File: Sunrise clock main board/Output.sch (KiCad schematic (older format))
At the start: 20 parts, among them J2 Screw terminal/dnf, J3 Screw terminal/dnf, J4 Conn_02x05_Odd_Even, Q2 IRML2244, U7 74AHC125D

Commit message: Tweaks
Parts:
- F1: footprint Fuse:Fuse_1812_4532Metric_Pad1.30x3.40mm_HandSolder -> Fuse-fixed:Fuse_1812_4532Metric_Pad1.30x3.40mm_HandSolder
- L1: footprint Inductor-extra:L_12x12mm_H8mm-L_Radial_D10.0mm_P5.00mm -> Inductor-fixed:L_12x12mm_H8mm
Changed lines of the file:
@@
 F 0 "F1" V 7375 3100 50  0000 C CNN
 F 1 "Polyfuse 1.5A >=6V" V 7466 3100 50  0000 C CNN
-F 2 "Fuse:Fuse_1812_4532Metric_Pad1.30x3.40mm_HandSolder" H 7650 2900 50  0001 L CNN
+F 2 "Fuse-fixed:Fuse_1812_4532Metric_Pad1.30x3.40mm_HandSolder" H 7650 2900 50  0001 L CNN
 F 3 "~" H 7600 3100 50  0001 C CNN
 	1    7600 3100
@@
 F 0 "L1" V 6675 3100 50  0000 C CNN
 F 1 "22uH 3A" V 6584 3100 50  0000 C CNN
-F 2 "Inductor-extra:L_12x12mm_H8mm-L_Radial_D10.0mm_P5.00mm" H 6450 3100 50  0001 C CNN
+F 2 "Inductor-fixed:L_12x12mm_H8mm" H 6450 3100 50  0001 C CNN
 F 3 "~" H 6450 3100 50  0001 C CNN
 	1    6450 3100

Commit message: Now in stereo if you want.
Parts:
- removed J2: Screw terminal/dnf, TerminalBlock_Phoenix:TerminalBlock_Phoenix_MKDS-1,5-2-5.08_1x02_P5.08mm_Horizontal, symbol Connector:Screw_Terminal_01x02
- removed R63: 100k, Resistor_SMD:R_0805_2012Metric_Pad1.20x1.40mm_HandSolder, symbol Device:R
- added A4: max98357, Module-extra:max98357, symbol Module-extra:max98357
- added D5, D6: BAV99, Package_TO_SOT_SMD:SOT-23, symbol Diode:BAV99
- added Q1: IRML2244, Package_TO_SOT_SMD:SOT-23, symbol Device:Q_PMOS_GSD
- added Q3, Q4: 2N7002, Package_TO_SOT_SMD:SOT-23, symbol Transistor_FET:2N7002
- added R14, R16: 100R, Resistor_SMD:R_0805_2012Metric_Pad1.20x1.40mm_HandSolder, symbol Device:R
- added R62, R66, R69, R70: 100k, Resistor_SMD:R_0805_2012Metric_Pad1.20x1.40mm_HandSolder, symbol Device:R
- added R79: 560k, Resistor_SMD:R_0805_2012Metric_Pad1.20x1.40mm_HandSolder, symbol Device:R
- J3: footprint TerminalBlock_Phoenix:TerminalBlock_Phoenix_MKDS-1,5-3-5.08_1x03_P5.08mm_Horizontal -> TerminalBlock_Phoenix:TerminalBlock_Phoenix_MKDS-1,5-5-5.08_1x05_P5.08mm_Horizontal; symbol Connector:Screw_Terminal_01x03 -> Connector:Screw_Terminal_01x05
- NT1: footprint NetTie:NetTie-2_SMD_Pad0.5mm -> NetTie-fixed:NetTie-2_SMD_Pad0.5mm
- R63: renamed from R41; value 10k -> 100k
- renumbered R14 to R1
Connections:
- net labels added: EXTERNAL_GND, GPIO1, GPO2, GPO2_5V, I2S_GAIN0, I2S_GAIN1, ~SDL, ~SDR
- net labels removed: I2S_GAIN, NEOPIXEL_GND, SPK+, SPK-
- wire segments 92 -> 146
- no-connect marks 0 -> 5
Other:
- note added: "Audio amplifier module"
- note added: "Connect to pins 1 to 5\nof GX16-5 connector."
- note added: "Do not fit any components in this block if you want mono output"
- note added: "External interface for Neopixel and GP(I)O"
- note added: "Unused, but not forgotten"
- note added: "left channel or mono"
- note added: "right channel\n"
- note removed: "Connect to pin 1,2 and 3\nof GX16-5 connector."
- note removed: "MAX98357 I2S 3W audio amplifier module"
- note removed: "Neopixel"
- moved on the sheet: A3, C3, D3, D4, F1, J4, L1, NT1, Q2, R3, R4, R63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

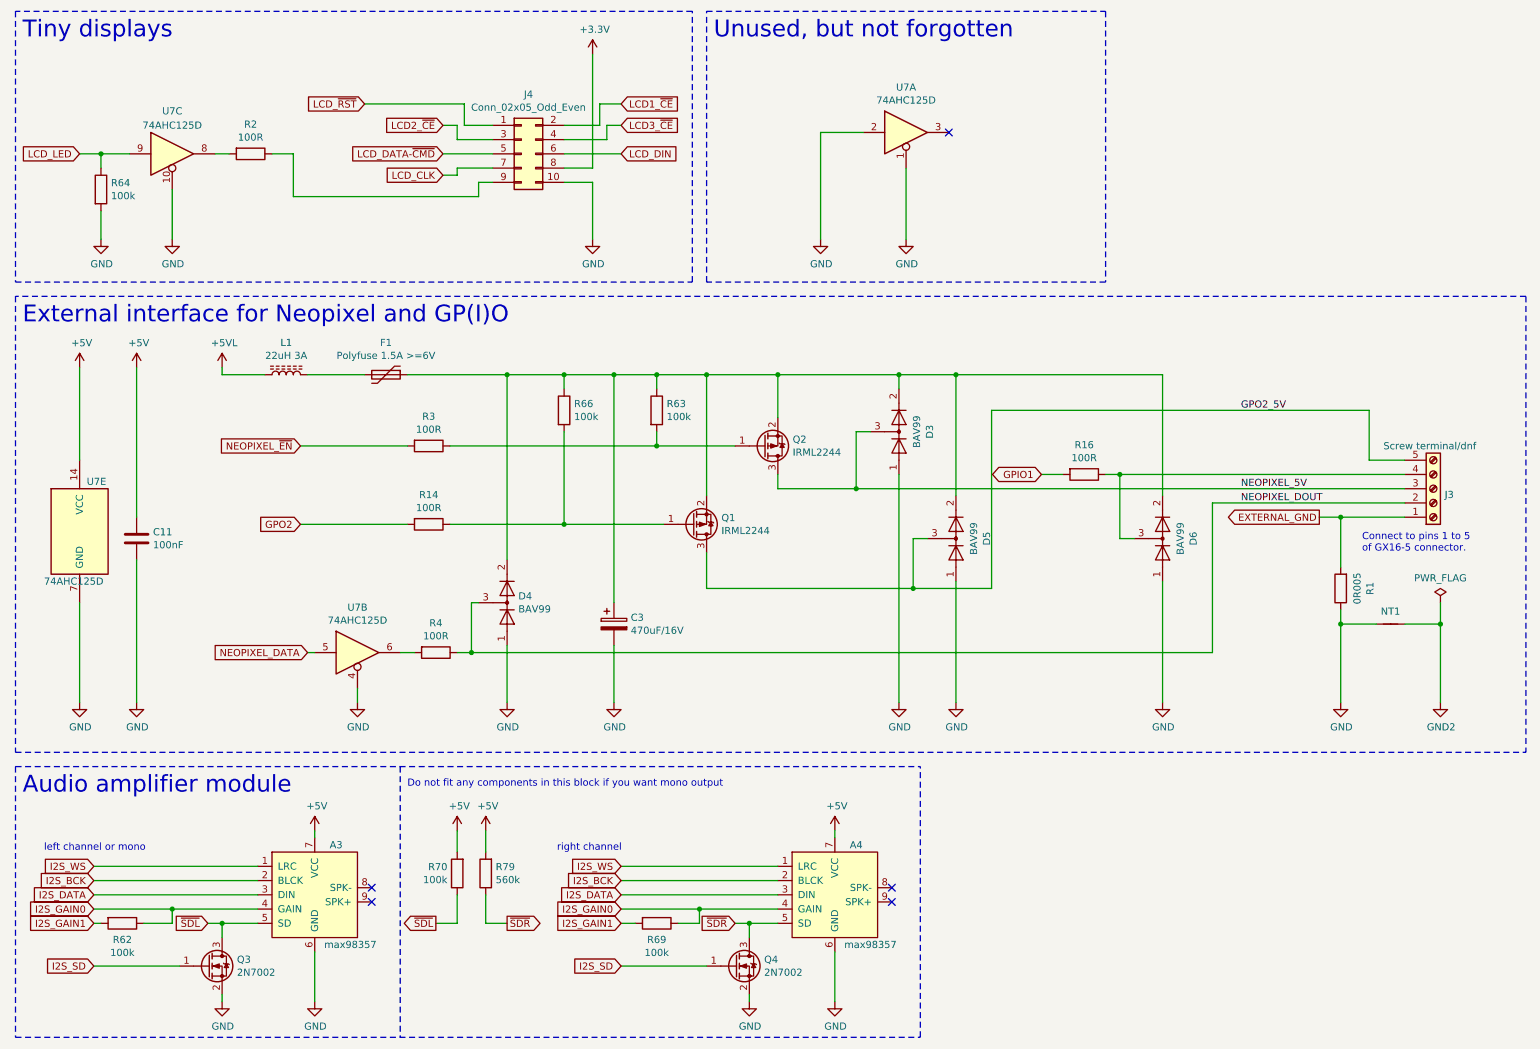
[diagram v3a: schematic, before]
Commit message: Started with checklist.
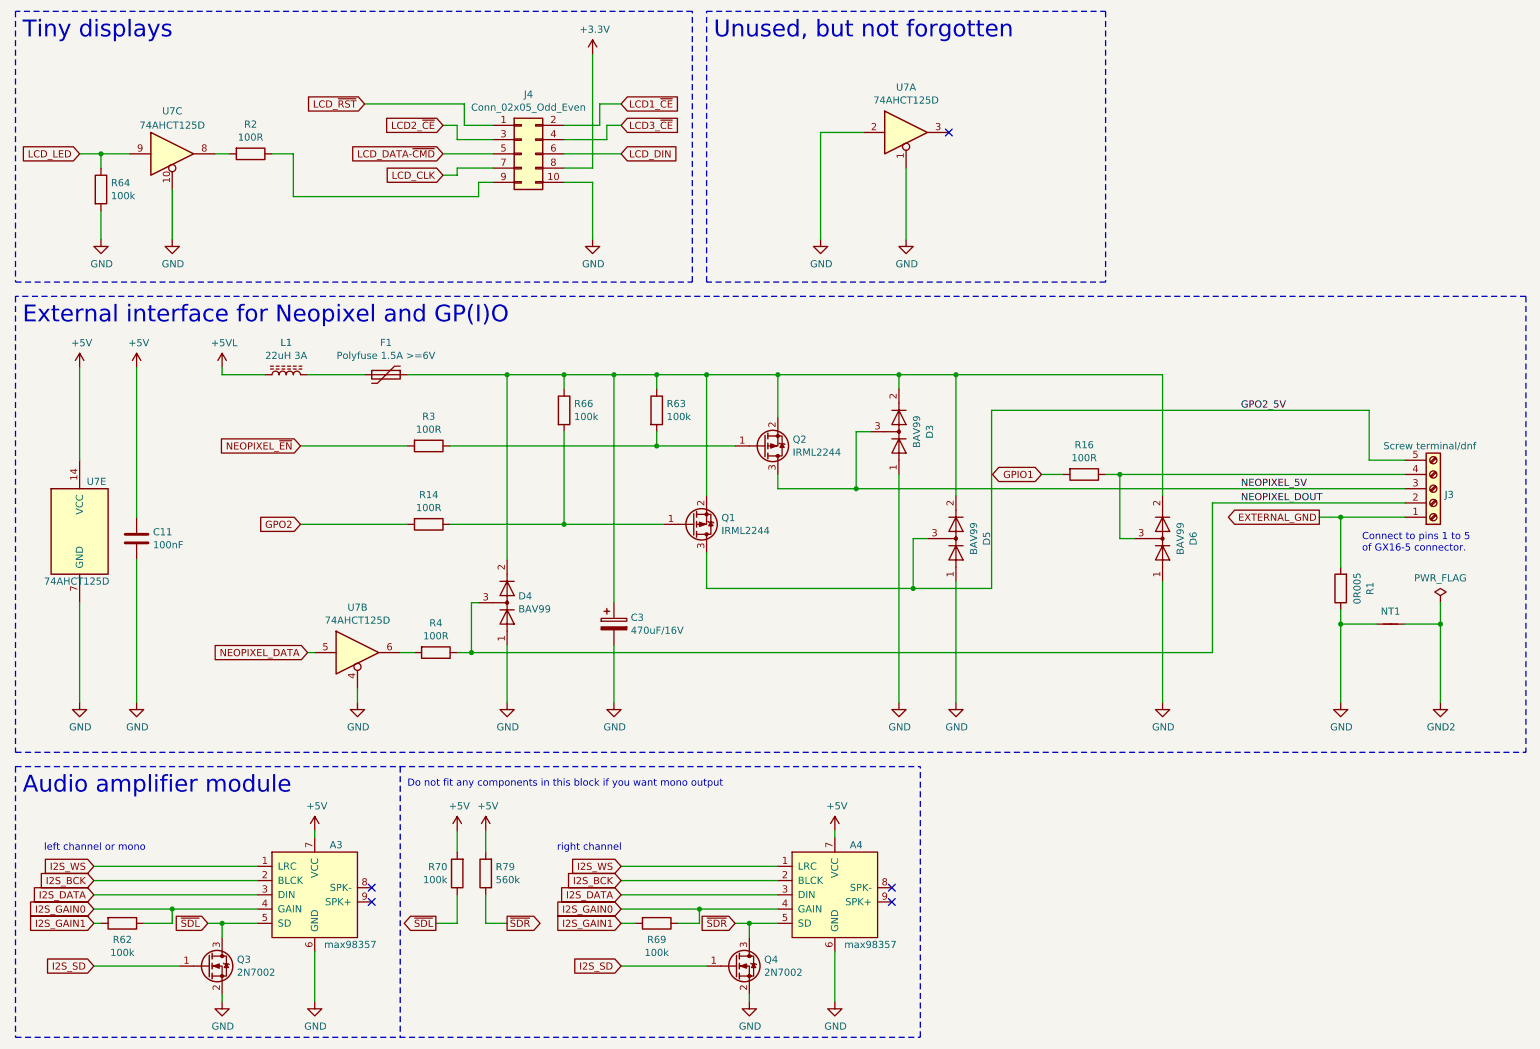
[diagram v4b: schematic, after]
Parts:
- U7: value 74AHC125D -> 74AHCT125D
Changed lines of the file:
@@
 AR Path="/5FF1E7F2/5FF38C00" Ref="U7"  Part="1"
 F 0 "U7" H 6800 1717 50  0000 C CNN
-F 1 "74AHC125D" H 6800 1626 50  0000 C CNN
+F 1 "74AHCT125D" H 6800 1626 50  0000 C CNN
 F 2 "Package_SO-fixed:SO-14_3.9x8.65mm_P1.27mm" H 6800 1400 50  0001 C CNN
 F 3 "" H 6800 1400 50  0001 C CNN
@@
 AR Path="/5FF1E7F2/5FF38C06" Ref="U7"  Part="2"
 F 0 "U7" H 2950 5367 50  0000 C CNN
-F 1 "74AHC125D" H 2950 5276 50  0000 C CNN
+F 1 "74AHCT125D" H 2950 5276 50  0000 C CNN
 F 2 "Package_SO-fixed:SO-14_3.9x8.65mm_P1.27mm" H 2950 5050 50  0001 C CNN
 F 3 "" H 2950 5050 50  0001 C CNN
@@
 AR Path="/5FF1E7F2/5FF38C0C" Ref="U7"  Part="3"
 F 0 "U7" H 1650 1850 50  0000 C CNN
-F 1 "74AHC125D" H 1650 1750 50  0000 C CNN
+F 1 "74AHCT125D" H 1650 1750 50  0000 C CNN
 F 2 "Package_SO-fixed:SO-14_3.9x8.65mm_P1.27mm" H 1650 1550 50  0001 C CNN
 F 3 "" H 1650 1550 50  0001 C CNN
@@
 AR Path="/5FF1E7F2/5FF38C18" Ref="U7"  Part="5"
 F 0 "U7" H 1050 4550 50  0000 L CNN
-F 1 "74AHC125D" H 750 3850 50  0000 L CNN
+F 1 "74AHCT125D" H 750 3850 50  0000 L CNN
 F 2 "Package_SO-fixed:SO-14_3.9x8.65mm_P1.27mm" H 1000 4200 50  0001 C CNN
 F 3 "" H 1000 4200 50  0001 C CNN

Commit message: More testing.
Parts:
- removed NT1: Net-Tie_2, NetTie-fixed:NetTie-2_SMD_Pad0.5mm, symbol Device:Net-Tie_2
- removed R1: 0R005, Resistor_SMD:R_2512_6332Metric_Pad1.52x3.35mm_HandSolder, symbol Device:R
- renumbered R16 to R13
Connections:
- net EXTERNAL_GND is gone; now on net GND: J3.1 (Pin_1)
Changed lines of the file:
@@
 Sheet 3 6
 Title "Sunrise clock main board"
-Date "2021-04-11"
-Rev "V1.0"
+Date "2021-05-04"
+Rev "V1.1"
 Comp "https://github.com/atoomnetmarc/Sunrise-clock-hardware"
 Comment1 ""
@@
 $EndComp
 Wire Wire Line
-	9850 5400 9850 4850
-Wire Wire Line
 	9850 4100 10300 4100
 Wire Wire Line
@@
 Text Notes 10000 4350 0    50   ~ 0
 Connect to pins 1 to 5\nof GX16-5 connector.
-$Comp
-L Device:R R?
-U 1 1 5FF8F584
-P 9850 4600
-AR Path="/5FF8F584" Ref="R?"  Part="1"
-AR Path="/5FF1E7F2/5FF8F584" Ref="R1"  Part="1"
-F 0 "R1" V 9643 4600 50  0000 C CNN
-F 1 "0R005" V 9734 4600 50  0000 C CNN
-F 2 "Resistor_SMD:R_2512_6332Metric_Pad1.52x3.35mm_HandSolder" V 9780 4600 50  0001 C CNN
-F 3 "~" H 9850 4600 50  0001 C CNN
-	1    9850 4600
-	-1   0    0    1
-$EndComp
-Wire Wire Line
-	9850 4450 9850 4100
-Text GLabel 9700 4100 0    50   Output ~ 0
-EXTERNAL_GND
-Wire Wire Line
-	9850 4100 9700 4100
-Connection ~ 9850 4100
-$Comp
-L power:GND2 #PWR040
-U 1 1 5FFE3A4B
-P 10550 5400
-F 0 "#PWR040" H 10550 5150 50  0001 C CNN
-F 1 "GND2" H 10555 5227 50  0000 C CNN
-F 2 "" H 10550 5400 50  0001 C CNN
-F 3 "" H 10550 5400 50  0001 C CNN
-	1    10550 5400
-	1    0    0    -1
-$EndComp
-Wire Wire Line
-	10100 4850 9850 4850
-Connection ~ 9850 4850
-Wire Wire Line
-	9850 4850 9850 4750
-Wire Wire Line
-	10300 4850 10550 4850
-Wire Wire Line
-	10550 4850 10550 5400
-$Comp
-L power:PWR_FLAG #FLG01
-U 1 1 5FFE9589
-P 10550 4700
-F 0 "#FLG01" H 10550 4775 50  0001 C CNN
-F 1 "PWR_FLAG" H 10550 4873 50  0000 C CNN
-F 2 "" H 10550 4700 50  0001 C CNN
-F 3 "~" H 10550 4700 50  0001 C CNN
-	1    10550 4700
-	1    0    0    -1
-$EndComp
-Wire Wire Line
-	10550 4850 10550 4700
-Connection ~ 10550 4850
 Wire Wire Line
 	3000 1200 3700 1200
@@
 P 8050 3800
 AR Path="/6083B3D8" Ref="R?"  Part="1"
-AR Path="/5FF1E7F2/6083B3D8" Ref="R16"  Part="1"
-F 0 "R16" V 7843 3800 50  0000 C CNN
+AR Path="/5FF1E7F2/6083B3D8" Ref="R13"  Part="1"
+F 0 "R13" V 7843 3800 50  0000 C CNN
 F 1 "100R" V 7934 3800 50  0000 C CNN
 F 2 "Resistor_SMD:R_0805_2012Metric_Pad1.20x1.40mm_HandSolder" V 7980 3800 50  0001 C CNN
@@
 Text Notes 5450 750  0    118  ~ 0
 Unused, but not forgotten
-$Comp
-L Device:Net-Tie_2 NT1
-U 1 1 5FFE41C2
-P 10200 4850
-F 0 "NT1" H 10200 4939 50  0000 C CNN
-F 1 "Net-Tie_2" H 10200 4940 50  0001 C CNN
-F 2 "NetTie-fixed:NetTie-2_SMD_Pad0.5mm" H 10200 4850 50  0001 C CNN
-F 3 "~" H 10200 4850 50  0001 C CNN
-	1    10200 4850
-	1    0    0    -1
-$EndComp
 NoConn ~ 3050 6700
 NoConn ~ 3050 6800
@@
 	5600 6950 5700 6950
 Connection ~ 5700 6950
+Wire Wire Line
+	9850 4100 9850 5400
 $EndSCHEMATC
